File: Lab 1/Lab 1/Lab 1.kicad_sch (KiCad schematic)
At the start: 18 parts, among them SW1 SW_Push, SW2 SW_Push_Open, SW3 SW_Push, SW4 SW_Push_Open

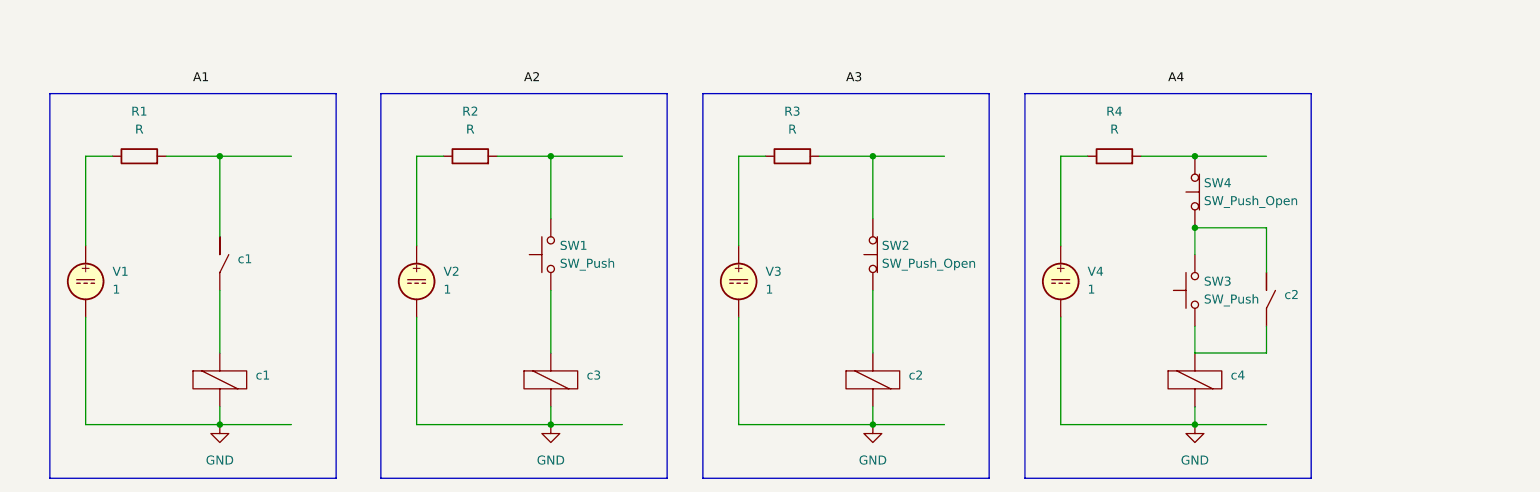
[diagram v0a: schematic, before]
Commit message: Fix lab A1-4
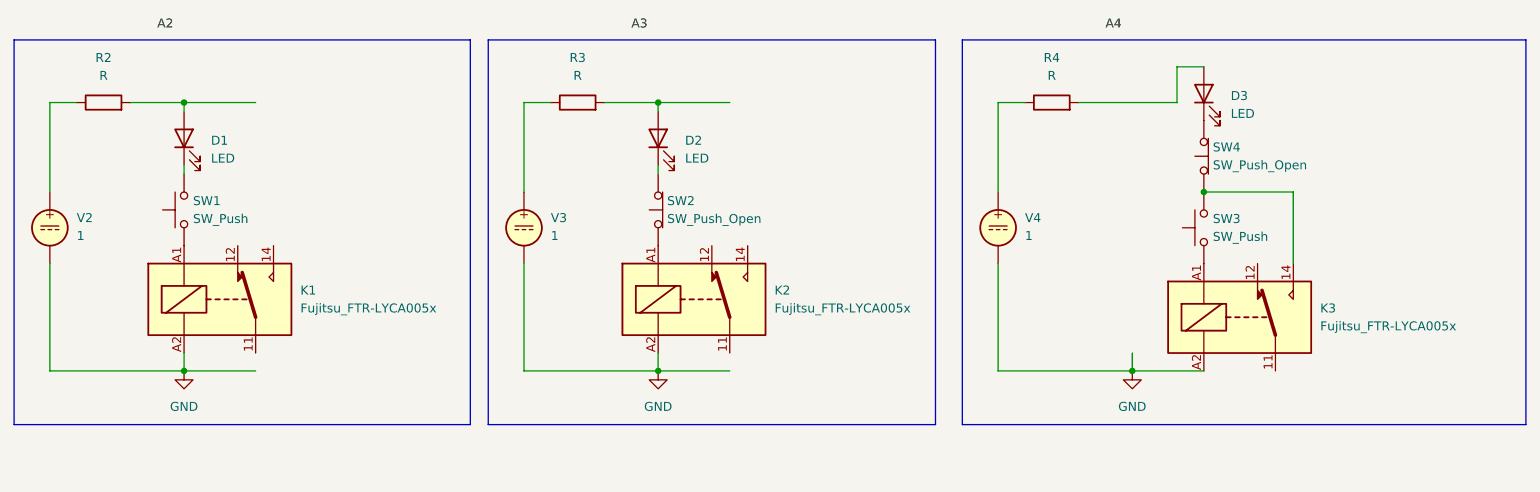
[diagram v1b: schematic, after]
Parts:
- removed R1: R, symbol Device:R
- removed V1: 1, symbol Simulation_SPICE:VDC
- removed c1, c2: ~, symbol relay_contact:Relay_contact
- removed c1, c2, c3, c4: ~, symbol relay_coil:Relay_coil
- added D1, D2, D3: LED, symbol Device:LED
- added K1, K2, K3: Fujitsu_FTR-LYCA005x, Relay_THT:Relay_SPDT_Fujitsu_FTR-LYCA005x_FormC_Vertical, symbol Relay:Fujitsu_FTR-LYCA005x
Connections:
- net GND: now also K1.A2, K2.A2, K3.A2
- net at R4.2: now also D3.2 (A); no longer SW4.2 (B)
- net at R3.2: now also D2.2 (A); no longer SW2.2 (B)
- net at SW2.1 (A): now also K2.A1
- net at R2.2: now also D1.2 (A); no longer SW1.2
- net at SW3.1: now also K3.A1
- net at SW3.2, SW4.1 (A): now also K3.14
- net at SW1.1: now also K1.A1
- new net: D2.1 (K), SW2.2 (B)
- new net: D1.1 (K), SW1.2
- new net: D3.1 (K), SW4.2 (B)
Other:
- moved on the sheet: R2, R3, R4, SW1, SW2, SW3, V2, V3, V4

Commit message: B1
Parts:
- added K4, K5, K6, K7: Fujitsu_FTR-LYCA005x, Relay_THT:Relay_SPDT_Fujitsu_FTR-LYCA005x_FormC_Vertical, symbol Relay:Fujitsu_FTR-LYCA005x
- added M1: Motor_DC, symbol Motor:Motor_DC
- added SW5, SW6: SW_Push, symbol Switch:SW_Push
- added V1: 1, symbol Simulation_SPICE:VDC
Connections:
- net GND: now also K4.A1, K5.11, K6.A1, K7.11, SW5.1, SW6.1, V1.2
- new net: K4.11, K5.A1, K6.11, K7.A1, V1.1
- new net: K6.14, K7.14, M1.2 (-)
- new net: K4.14, K5.14, M1.1 (+)
- new net Left: K5.A2, K6.A2, SW5.2
- new net Right: K4.A2, K7.A2, SW6.2

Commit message: Fix B1
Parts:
- added D4, D5: LED, symbol Device:LED
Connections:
- net GND: no longer K4.A1, K6.A1
- net at K4.11, K5.A1, K6.11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: now also K4.A1, K6.A1
- net at K6.14, M1.2 (-): now also D4.2 (A); no longer K7.14
- net at K4.14, M1.1 (+): now also D5.2 (A); no longer K5.14
- new net: D5.1 (K), K5.14
- new net: D4.1 (K), K7.14
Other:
- moved on the sheet: K5, K6, K7, V1

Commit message: Add B2
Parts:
- added D6, D7, D8: LED, symbol Device:LED
- added K10, K11, K8, K9: Fujitsu_FTR-LYCA005x, Relay_THT:Relay_SPDT_Fujitsu_FTR-LYCA005x_FormC_Vertical, symbol Relay:Fujitsu_FTR-LYCA005x
- added M2: Motor_DC, symbol Motor:Motor_DC
- added SW11, SW9: SW_Nidec_CAS-120A1, Button_Switch_SMD:Nidec_Copal_CAS-120A, symbol Switch:SW_Nidec_CAS-120A1
- added SW7, SW8: SW_Push, symbol Switch:SW_Push
- added V5: 1, symbol Simulation_SPICE:VDC
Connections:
- net GND: now also K11.11, K9.11, SW11.2 (B), SW9.2 (B), V5.2
- net Left: now also K10.A2, K9.A2, SW7.2
- net Right: now also K11.A2, K8.A2, SW8.2
- net at K6.14, M1.2 (-): now also D5.2 (A); no longer D4.2 (A)
- net at K4.14, M1.1 (+): now also D4.2 (A); no longer D5.2 (A)
- net at K5.14: now also D4.1 (K); no longer D5.1 (K)
- net at K7.14: now also D5.1 (K); no longer D4.1 (K)
- new net: D8.1 (K), SW11.1 (C), SW9.1 (C)
- new net: D8.2 (A), K10.11, K10.A1, K11.A1, K8.11, K8.A1, K9.A1, V5.1
- new net: SW7.1, SW9.3 (A)
- new net: D6.1 (K), K9.14
- new net: D6.2 (A), K8.14, M2.1 (+)
- new net: SW11.3 (A), SW8.1
- new net: D7.1 (K), K11.14
- new net: D7.2 (A), K10.14, M2.2 (-)

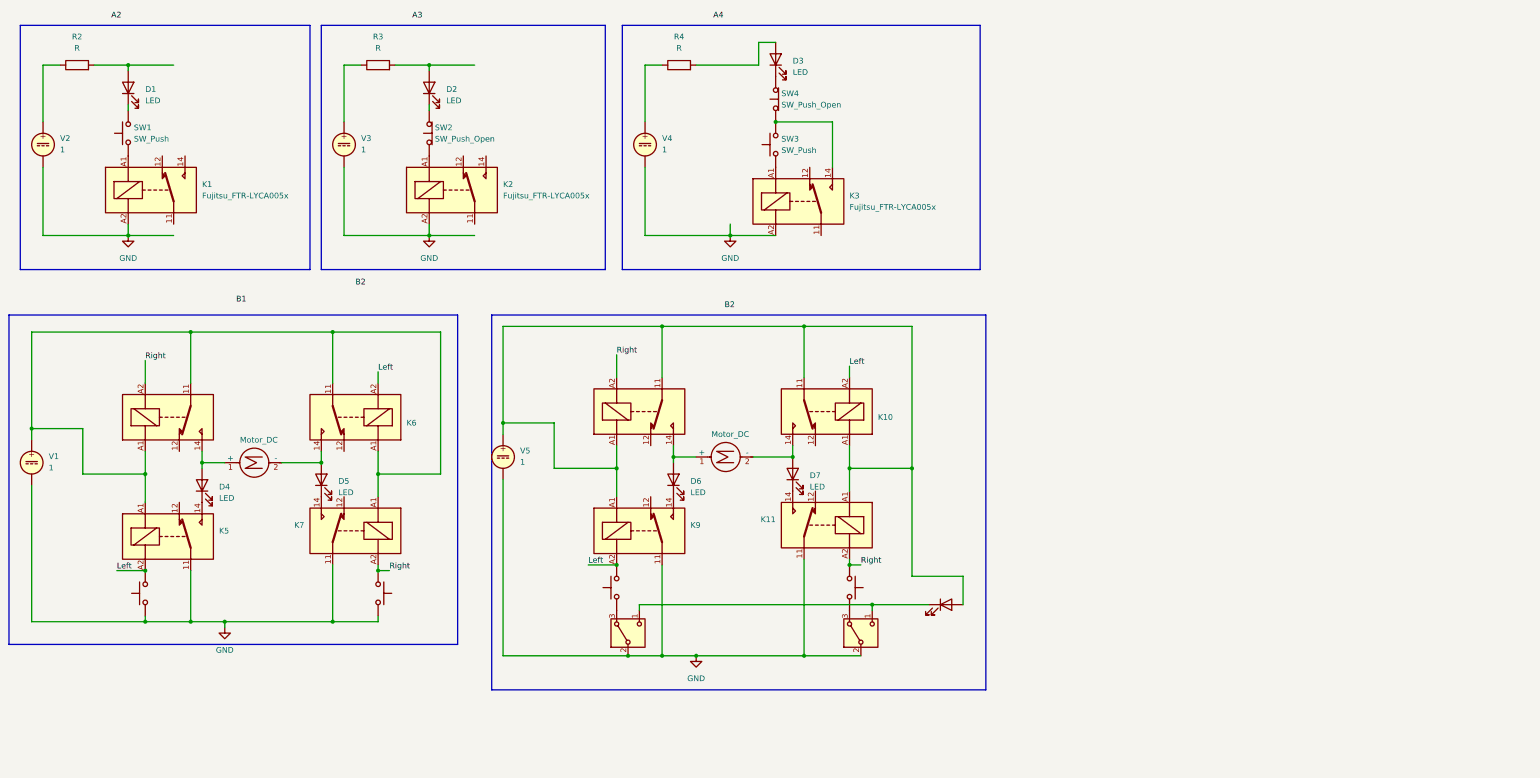
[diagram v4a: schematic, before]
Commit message: Add B3 possible solution without toggle
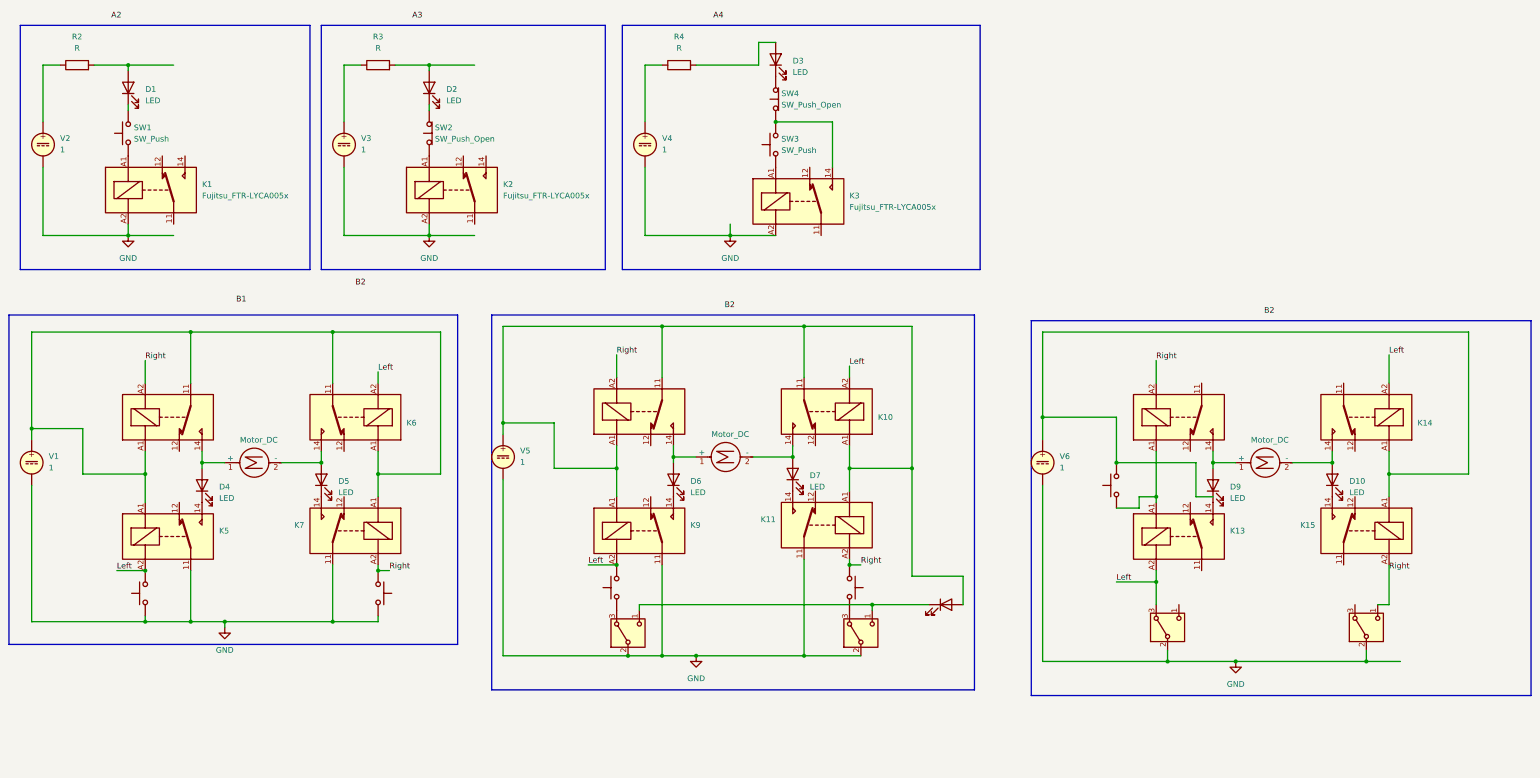
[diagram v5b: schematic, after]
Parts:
- added D10, D9: LED, symbol Device:LED
- added K12, K13, K14, K15: Fujitsu_FTR-LYCA005x, Relay_THT:Relay_SPDT_Fujitsu_FTR-LYCA005x_FormC_Vertical, symbol Relay:Fujitsu_FTR-LYCA005x
- added M3: Motor_DC, symbol Motor:Motor_DC
- added SW10, SW12: SW_Nidec_CAS-120A1, Button_Switch_SMD:Nidec_Copal_CAS-120A, symbol Switch:SW_Nidec_CAS-120A1
- added SW13: SW_Push, symbol Switch:SW_Push
- added V6: 1, symbol Simulation_SPICE:VDC
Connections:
- net GND: now also SW10.2 (B), SW12.2 (B), V6.2
- net Left: now also K13.A2, K14.A2, SW10.3 (A)
- net Right: now also K12.A2, K15.A2, SW12.1 (C)
- new net: D9.2 (A), K12.14, M3.1 (+)
- new net: D10.2 (A), K14.14, M3.2 (-)
- new net: K14.A1, K15.A1, SW13.2, V6.1
- new net: D10.1 (K), K15.14
- new net: D9.1 (K), K13.14
- new net: K12.A1, K13.A1, SW13.1
